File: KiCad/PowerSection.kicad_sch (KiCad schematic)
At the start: 28 parts, among them U2 MC34063AP, U3 LM7805_TO220, U4 LM337_TO220, U7 LM317_TO-220

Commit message: Changed footprints, arrangement of elements on pcb
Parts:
- removed R4, R46: 860, Resistor_SMD:R_0805_2012Metric_Pad1.20x1.40mm_HandSolder, symbol Device:R
- added R4, R46: 1k, Potentiometer_SMD:Potentiometer_Bourns_TC33X_Vertical, symbol Device:R_Variable
- C11, C12, C9: footprint Capacitor_SMD:CP_Elec_6.3x5.3 -> Capacitor_THT:CP_Radial_D5.0mm_P2.00mm
- C2, C4: footprint Capacitor_SMD:CP_Elec_6.3x7.7 -> Capacitor_THT:CP_Radial_D8.0mm_P3.50mm
- C6: footprint Capacitor_SMD:C_0805_2012Metric_Pad1.18x1.45mm_HandSolder -> Capacitor_THT:CP_Radial_D5.0mm_P2.00mm
- D2, D6, D7, D8: footprint Diode_SMD:D_SOD-123F -> Diode_THT:D_DO-41_SOD81_P10.16mm_Horizontal
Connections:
- net GND: now also R4.1, R46.2
- net at C6.1, D7.2 (A), R45.1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: now also R46.1
- net at C9.2, D8.1 (K), R5.2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: now also R4.2
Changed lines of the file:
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@@
 			)
 		)
-		(property "Footprint" "Capacitor_SMD:C_0805_2012Metric_Pad1.18x1.45mm_HandSolder"
+		(property "Footprint" "Capacitor_THT:CP_Radial_D5.0mm_P2.00mm"
 			(at 233.3752 91.44 0)
 			(effects
@@
 				(path "/e2db369b-fed9-4358-b449-15db5155edf2/27026b69-1c54-41be-a6f6-95a262163c29"
 					(reference "C10")
+					(unit 1)
+				)
+			)
+		)
+	)
+	(symbol
+		(lib_id "Device:R_Variable")
+		(at 209.55 119.38 0)
+		(unit 1)
+		(exclude_from_sim no)
+		(in_bom yes)
+		(on_board yes)
+		(dnp no)
+		(fields_autoplaced yes)
+		(property "Reference" "R4"
+			(at 213.36 118.1099 0)
+			(effects
+				(font
+					(size 1.27 1.27)
+				)
+				(justify left)
+			)
+		)
+		(property "Value" "1k"
+			(at 213.36 120.6499 0)
+			(effects
+				(font
+					(size 1.27 1.27)
+				)
+				(justify left)
+			)
+		)
+		(property "Footprint" "Potentiometer_SMD:Potentiometer_Bourns_TC33X_Vertical"
+			(at 207.772 119.38 90)
+			(effects
+				(font
+					(size 1.27 1.27)
+				)
+				(hide yes)
+			)
+		)
+		(property "Datasheet" "~"
+			(at 209.55 119.38 0)
+			(effects
+				(font
+					(size 1.27 1.27)
+				)
+				(hide yes)
+			)
+		)
+		(property "Description" "Variable resistor"
+			(at 209.55 119.38 0)
+			(effects
+				(font
+					(size 1.27 1.27)
+				)
+				(hide yes)
+			)
+		)
+		(pin "1"
+		)
+		(pin "2"
+		)
+		(instances
+			(project "SiganlGen"
+				(path "/e2db369b-fed9-4358-b449-15db5155edf2/27026b69-1c54-41be-a6f6-95a262163c29"
+					(reference "R4")
 					(unit 1)
 				)
@@
 	)
 	(symbol
-		(lib_id "Device:R")
-		(at 209.55 119.38 180)
-		(unit 1)
-		(exclude_from_sim no)
-		(in_bom yes)
-		(on_board yes)
-		(dnp no)
-		(fields_autoplaced yes)
-		(property "Reference" "R4"
-			(at 212.09 118.1099 0)
-			(effects
-				(font
-					(size 1.27 1.27)
-				)
-				(justify right)
-			)
-		)
-		(property "Value" "860"
-			(at 212.09 120.6499 0)
-			(effects
-				(font
-					(size 1.27 1.27)
-				)
-				(justify right)
-			)
-		)
-		(property "Footprint" "Resistor_SMD:R_0805_2012Metric_Pad1.20x1.40mm_HandSolder"
-			(at 211.328 119.38 90)
-			(effects
-				(font
-					(size 1.27 1.27)
-				)
-				(hide yes)
-			)
-		)
-		(property "Datasheet" "~"
-			(at 209.55 119.38 0)
-			(effects
-				(font
-					(size 1.27 1.27)
-				)
-				(hide yes)
-			)
-		)
-		(property "Description" "Resistor"
-			(at 209.55 119.38 0)
-			(effects
-				(font
-					(size 1.27 1.27)
-				)
-				(hide yes)
-			)
-		)
-		(pin "1"
-		)
-		(pin "2"
-		)
-		(instances
-			(project "SiganlGen"
-				(path "/e2db369b-fed9-4358-b449-15db5155edf2/27026b69-1c54-41be-a6f6-95a262163c29"
-					(reference "R4")
-					(unit 1)
-				)
-			)
-		)
-	)
-	(symbol
 		(lib_id "Device:C")
 		(at 104.14 111.76 0)
@@
 			)
 		)
-		(property "Footprint" "Capacitor_SMD:CP_Elec_6.3x5.3"
+		(property "Footprint" "Capacitor_THT:CP_Radial_D5.0mm_P2.00mm"
 			(at 246.0752 86.36 0)
 			(effects
@@
 			)
 		)
-		(property "Footprint" "Diode_SMD:D_SOD-123F"
+		(property "Footprint" "Diode_THT:D_DO-41_SOD81_P10.16mm_Horizontal"
 			(at 209.55 64.135 0)
 			(effects
@@
 			)
 		)
-		(property "Footprint" "Capacitor_SMD:CP_Elec_6.3x7.7"
+		(property "Footprint" "Capacitor_THT:CP_Radial_D8.0mm_P3.50mm"
 			(at 89.8652 102.87 0)
 			(effects
@@
 	)
 	(symbol
-		(lib_id "Device:R")
-		(at 209.55 88.9 180)
+		(lib_id "Device:R_Variable")
+		(at 209.55 88.9 0)
 		(unit 1)
 		(exclude_from_sim no)
@@
 		(fields_autoplaced yes)
 		(property "Reference" "R46"
-			(at 212.09 87.6299 0)
-			(effects
-				(font
-					(size 1.27 1.27)
-				)
-				(justify right)
-			)
-		)
-		(property "Value" "860"
-			(at 212.09 90.1699 0)
-			(effects
-				(font
-					(size 1.27 1.27)
-				)
-				(justify right)
-			)
-		)
-		(property "Footprint" "Resistor_SMD:R_0805_2012Metric_Pad1.20x1.40mm_HandSolder"
-			(at 211.328 88.9 90)
+			(at 213.36 87.6299 0)
+			(effects
+				(font
+					(size 1.27 1.27)
+				)
+				(justify left)
+			)
+		)
+		(property "Value" "1k"
+			(at 213.36 90.1699 0)
+			(effects
+				(font
+					(size 1.27 1.27)
+				)
+				(justify left)
+			)
+		)
+		(property "Footprint" "Potentiometer_SMD:Potentiometer_Bourns_TC33X_Vertical"
+			(at 207.772 88.9 90)
 			(effects
 				(font
@@
 			)
 		)
-		(property "Description" "Resistor"
+		(property "Description" "Variable resistor"
 			(at 209.55 88.9 0)
 			(effects
@@
 			)
 		)
-		(property "Footprint" "Diode_SMD:D_SOD-123F"
+		(property "Footprint" "Diode_THT:D_DO-41_SOD81_P10.16mm_Horizontal"
 			(at 227.965 77.47 0)
 			(effects
@@
 			)
 		)
-		(property "Footprint" "Diode_SMD:D_SOD-123F"
+		(property "Footprint" "Diode_THT:D_DO-41_SOD81_P10.16mm_Horizontal"
 			(at 227.965 130.81 0)
 			(effects
@@
 			)
 		)
-		(property "Footprint" "Diode_SMD:D_SOD-123F"
+		(property "Footprint" "Diode_THT:D_DO-41_SOD81_P10.16mm_Horizontal"
 			(at 207.01 142.875 0)
 			(effects
@@
 			)
 		)
-		(property "Footprint" "Capacitor_SMD:CP_Elec_6.3x7.7"
+		(property "Footprint" "Capacitor_THT:CP_Radial_D8.0mm_P3.50mm"
 			(at 149.5552 123.19 0)
 			(effects
@@
 			)
 		)
-		(property "Footprint" "Capacitor_SMD:CP_Elec_6.3x5.3"
+		(property "Footprint" "Capacitor_THT:CP_Radial_D5.0mm_P2.00mm"
 			(at 246.0752 130.81 0)
 			(effects
@@
 			)
 		)
-		(property "Footprint" "Capacitor_SMD:CP_Elec_6.3x5.3"
+		(property "Footprint" "Capacitor_THT:CP_Radial_D5.0mm_P2.00mm"
 			(at 233.3752 123.19 0)
 			(effects

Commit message: Tidied up schematic, changed footprints
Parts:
- D2, D6, D7, D8: footprint Diode_THT:D_DO-41_SOD81_P10.16mm_Horizontal -> Diode_SMD:D_SOD-123F
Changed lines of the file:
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@@
 			)
 		)
-		(property "Footprint" "Diode_THT:D_DO-41_SOD81_P10.16mm_Horizontal"
+		(property "Footprint" "Diode_SMD:D_SOD-123F"
 			(at 209.55 64.135 0)
 			(effects
@@
 			)
 		)
-		(property "Footprint" "Diode_THT:D_DO-41_SOD81_P10.16mm_Horizontal"
+		(property "Footprint" "Diode_SMD:D_SOD-123F"
 			(at 227.965 77.47 0)
 			(effects
@@
 			)
 		)
-		(property "Footprint" "Diode_THT:D_DO-41_SOD81_P10.16mm_Horizontal"
+		(property "Footprint" "Diode_SMD:D_SOD-123F"
 			(at 227.965 130.81 0)
 			(effects
@@
 			)
 		)
-		(property "Footprint" "Diode_THT:D_DO-41_SOD81_P10.16mm_Horizontal"
+		(property "Footprint" "Diode_SMD:D_SOD-123F"
 			(at 207.01 142.875 0)
 			(effects

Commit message: Alfa version of PCB design
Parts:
- removed C11, C12: 22u, Capacitor_THT:CP_Radial_D5.0mm_P2.00mm, symbol Device:C
- removed C2, C4: 220u, Capacitor_THT:CP_Radial_D8.0mm_P3.50mm, symbol Device:C
- added C11, C12, C13, C17: 100u, Capacitor_THT:CP_Radial_D5.0mm_P2.50mm, symbol Device:C_Polarized
- C6, C9: value 22u -> 10u; footprint Capacitor_THT:CP_Radial_D5.0mm_P2.00mm -> Capacitor_SMD:C_0805_2012Metric_Pad1.18x1.45mm_HandSolder
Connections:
- net +10V: now also C11.1
- net +12V: now also C17.1
- net -10V: now also C13.2
- net -12V: now also C12.2
- net GND: now also C11.2, C12.1, C13.1, C17.2

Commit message: PCB design
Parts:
- renumbered C9 to C10, C13 to C12, C5 to C2, C8 to C3, C17 to C4, C3 to C5, C12 to C6, C10 to C7, C7 to C8, C6 to C9, D1 to D2, D2 to D3, D6 to D4, D7 to D5, D8 to D6, R46 to R4, R4 to R5, R45 to R6, R5 to R7, U3 to U2, U2 to U3, U7 to U4, U4 to U5
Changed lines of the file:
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@@
 		(dnp no)
 		(fields_autoplaced yes)
-		(property "Reference" "U7"
+		(property "Reference" "U4"
 			(at 209.55 63.5 0)
 			(effects
@@
 			(project "SiganlGen"
 				(path "/e2db369b-fed9-4358-b449-15db5155edf2/27026b69-1c54-41be-a6f6-95a262163c29"
-					(reference "U7")
+					(reference "U4")
 					(unit 1)
 				)
@@
 		(dnp no)
 		(fields_autoplaced yes)
-		(property "Reference" "C6"
+		(property "Reference" "C9"
 			(at 236.22 86.3599 0)
 			(effects
@@
 			(project "SiganlGen"
 				(path "/e2db369b-fed9-4358-b449-15db5155edf2/27026b69-1c54-41be-a6f6-95a262163c29"
-					(reference "C6")
+					(reference "C9")
 					(unit 1)
 				)
@@
 		(on_board yes)
 		(dnp no)
-		(property "Reference" "C10"
+		(property "Reference" "C7"
 			(at 191.008 81.28 0)
 			(effects
@@
 			(project "SiganlGen"
 				(path "/e2db369b-fed9-4358-b449-15db5155edf2/27026b69-1c54-41be-a6f6-95a262163c29"
-					(reference "C10")
+					(reference "C7")
 					(unit 1)
 				)
@@
 		(dnp no)
 		(fields_autoplaced yes)
-		(property "Reference" "R4"
+		(property "Reference" "R5"
 			(at 213.36 118.1099 0)
 			(effects
@@
 			(project "SiganlGen"
 				(path "/e2db369b-fed9-4358-b449-15db5155edf2/27026b69-1c54-41be-a6f6-95a262163c29"
-					(reference "R4")
+					(reference "R5")
 					(unit 1)
 				)
@@
 		(on_board yes)
 		(dnp no)
-		(property "Reference" "U4"
+		(property "Reference" "U5"
 			(at 209.55 140.97 0)
 			(effects
@@
 			(project "SiganlGen"
 				(path "/e2db369b-fed9-4358-b449-15db5155edf2/27026b69-1c54-41be-a6f6-95a262163c29"
-					(reference "U4")
+					(reference "U5")
 					(unit 1)
 				)
@@
 		(on_board yes)
 		(dnp no)
-		(property "Reference" "C7"
+		(property "Reference" "C8"
 			(at 191.008 125.73 0)
 			(effects
@@
 			(project "SiganlGen"
 				(path "/e2db369b-fed9-4358-b449-15db5155edf2/27026b69-1c54-41be-a6f6-95a262163c29"
-					(reference "C7")
+					(reference "C8")
 					(unit 1)
 				)
@@
 		(dnp no)
 		(fields_autoplaced yes)
-		(property "Reference" "R5"
+		(property "Reference" "R7"
 			(at 223.52 129.5399 0)
 			(effects
@@
 			(project "SiganlGen"
 				(path "/e2db369b-fed9-4358-b449-15db5155edf2/27026b69-1c54-41be-a6f6-95a262163c29"
-					(reference "R5")
+					(reference "R7")
 					(unit 1)
 				)
@@
 		(dnp no)
 		(fields_autoplaced yes)
-		(property "Reference" "C3"
+		(property "Reference" "C5"
 			(at 107.95 110.4899 0)
 			(effects
@@
 			(project "SiganlGen"
 				(path "/e2db369b-fed9-4358-b449-15db5155edf2/27026b69-1c54-41be-a6f6-95a262163c29"
-					(reference "C3")
+					(reference "C5")
 					(unit 1)
 				)
@@
 		(dnp no)
 		(fields_autoplaced yes)
-		(property "Reference" "U2"
+		(property "Reference" "U3"
 			(at 118.11 83.82 0)
 			(effects
@@
 			(project "SiganlGen"
 				(path "/e2db369b-fed9-4358-b449-15db5155edf2/27026b69-1c54-41be-a6f6-95a262163c29"
-					(reference "U2")
+					(reference "U3")
 					(unit 1)
 				)
@@
 		(dnp no)
 		(fields_autoplaced yes)
-		(property "Reference" "C13"
+		(property "Reference" "C12"
 			(at 248.92 124.8409 0)
 			(effects
@@
 			(project "SiganlGen"
 				(path "/e2db369b-fed9-4358-b449-15db5155edf2/27026b69-1c54-41be-a6f6-95a262163c29"
-					(reference "C13")
+					(reference "C12")
 					(unit 1)
 				)
@@
 		(dnp no)
 		(fields_autoplaced yes)
-		(property "Reference" "C8"
+		(property "Reference" "C3"
 			(at 69.85 104.1399 0)
 			(effects
@@
 			(project "SiganlGen"
 				(path "/e2db369b-fed9-4358-b449-15db5155edf2/27026b69-1c54-41be-a6f6-95a262163c29"
-					(reference "C8")
+					(reference "C3")
 					(unit 1)
 				)
@@
 		(dnp no)
 		(fields_autoplaced yes)
-		(property "Reference" "U3"
+		(property "Reference" "U2"
 			(at 53.34 92.71 0)
 			(effects
@@
 			(project "SiganlGen"
 				(path "/e2db369b-fed9-4358-b449-15db5155edf2/27026b69-1c54-41be-a6f6-95a262163c29"
-					(reference "U3")
+					(reference "U2")
 					(unit 1)
 				)
@@
 		(dnp no)
 		(fields_autoplaced yes)
-		(property "Reference" "D6"
+		(property "Reference" "D4"
 			(at 209.55 53.34 0)
 			(effects
@@
 			(project "SiganlGen"
 				(path "/e2db369b-fed9-4358-b449-15db5155edf2/27026b69-1c54-41be-a6f6-95a262163c29"
-					(reference "D6")
+					(reference "D4")
 					(unit 1)
 				)
@@
 		(dnp no)
 		(fields_autoplaced yes)
-		(property "Reference" "R46"
+		(property "Reference" "R4"
 			(at 213.36 87.6299 0)
 			(effects
@@
 			(project "SiganlGen"
 				(path "/e2db369b-fed9-4358-b449-15db5155edf2/27026b69-1c54-41be-a6f6-95a262163c29"
-					(reference "R46")
+					(reference "R4")
 					(unit 1)
 				)
@@
 		(on_board yes)
 		(dnp no)
-		(property "Reference" "C12"
+		(property "Reference" "C6"
 			(at 143.51 122.936 0)
 			(effects
@@
 			(project "SiganlGen"
 				(path "/e2db369b-fed9-4358-b449-15db5155edf2/27026b69-1c54-41be-a6f6-95a262163c29"
-					(reference "C12")
+					(reference "C6")
 					(unit 1)
 				)
@@
 		(dnp no)
 		(fields_autoplaced yes)
-		(property "Reference" "D7"
+		(property "Reference" "D5"
 			(at 234.95 76.1999 90)
 			(effects
@@
 			(project "SiganlGen"
 				(path "/e2db369b-fed9-4358-b449-15db5155edf2/27026b69-1c54-41be-a6f6-95a262163c29"
-					(reference "D7")
+					(reference "D5")
 					(unit 1)
 				)
@@
 		(dnp no)
 		(fields_autoplaced yes)
-		(property "Reference" "D8"
+		(property "Reference" "D6"
 			(at 234.95 129.5399 90)
 			(effects
@@
 			(project "SiganlGen"
 				(path "/e2db369b-fed9-4358-b449-15db5155edf2/27026b69-1c54-41be-a6f6-95a262163c29"
-					(reference "D8")
+					(reference "D6")
 					(unit 1)
 				)
@@
 		(on_board yes)
 		(dnp no)
-		(property "Reference" "C5"
+		(property "Reference" "C2"
 			(at 42.672 103.886 0)
 			(effects
@@
 			(project "SiganlGen"
 				(path "/e2db369b-fed9-4358-b449-15db5155edf2/27026b69-1c54-41be-a6f6-95a262163c29"
-					(reference "C5")
+					(reference "C2")
 					(unit 1)
 				)
@@
 		(on_board yes)
 		(dnp no)
-		(property "Reference" "D2"
+		(property "Reference" "D3"
 			(at 210.82 148.59 0)
 			(effects
@@
 			(project "SiganlGen"
 				(path "/e2db369b-fed9-4358-b449-15db5155edf2/27026b69-1c54-41be-a6f6-95a262163c29"
-					(reference "D2")
+					(reference "D3")
 					(unit 1)
 				)
@@
 		(dnp no)
 		(fields_autoplaced yes)
-		(property "Reference" "D1"
+		(property "Reference" "D2"
 			(at 147.0025 95.25 0)
 			(effects
@@
 			(project "SiganlGen"
 				(path "/e2db369b-fed9-4358-b449-15db5155edf2/27026b69-1c54-41be-a6f6-95a262163c29"
-					(reference "D1")
+					(reference "D2")
 					(unit 1)
 				)
@@
 		(dnp no)
 		(fields_autoplaced yes)
-		(property "Reference" "R45"
+		(property "Reference" "R6"
 			(at 223.52 74.9299 0)
 			(effects
@@
 			(project "SiganlGen"
 				(path "/e2db369b-fed9-4358-b449-15db5155edf2/27026b69-1c54-41be-a6f6-95a262163c29"
-					(reference "R45")
+					(reference "R6")
 					(unit 1)
 				)
@@
 		(on_board yes)
 		(dnp no)
-		(property "Reference" "C9"
+		(property "Reference" "C10"
 			(at 235.458 118.364 0)
 			(effects
@@
 			(project "SiganlGen"
 				(path "/e2db369b-fed9-4358-b449-15db5155edf2/27026b69-1c54-41be-a6f6-95a262163c29"
-					(reference "C9")
+					(reference "C10")
 					(unit 1)
 				)
@@
 		(dnp no)
 		(fields_autoplaced yes)
-		(property "Reference" "C17"
+		(property "Reference" "C4"
 			(at 92.71 96.9009 0)
 			(effects
@@
 			(project "SiganlGen"
 				(path "/e2db369b-fed9-4358-b449-15db5155edf2/27026b69-1c54-41be-a6f6-95a262163c29"
-					(reference "C17")
-					(unit 1)
-				)
+					(reference "C4")
+					(unit 1)
+				)

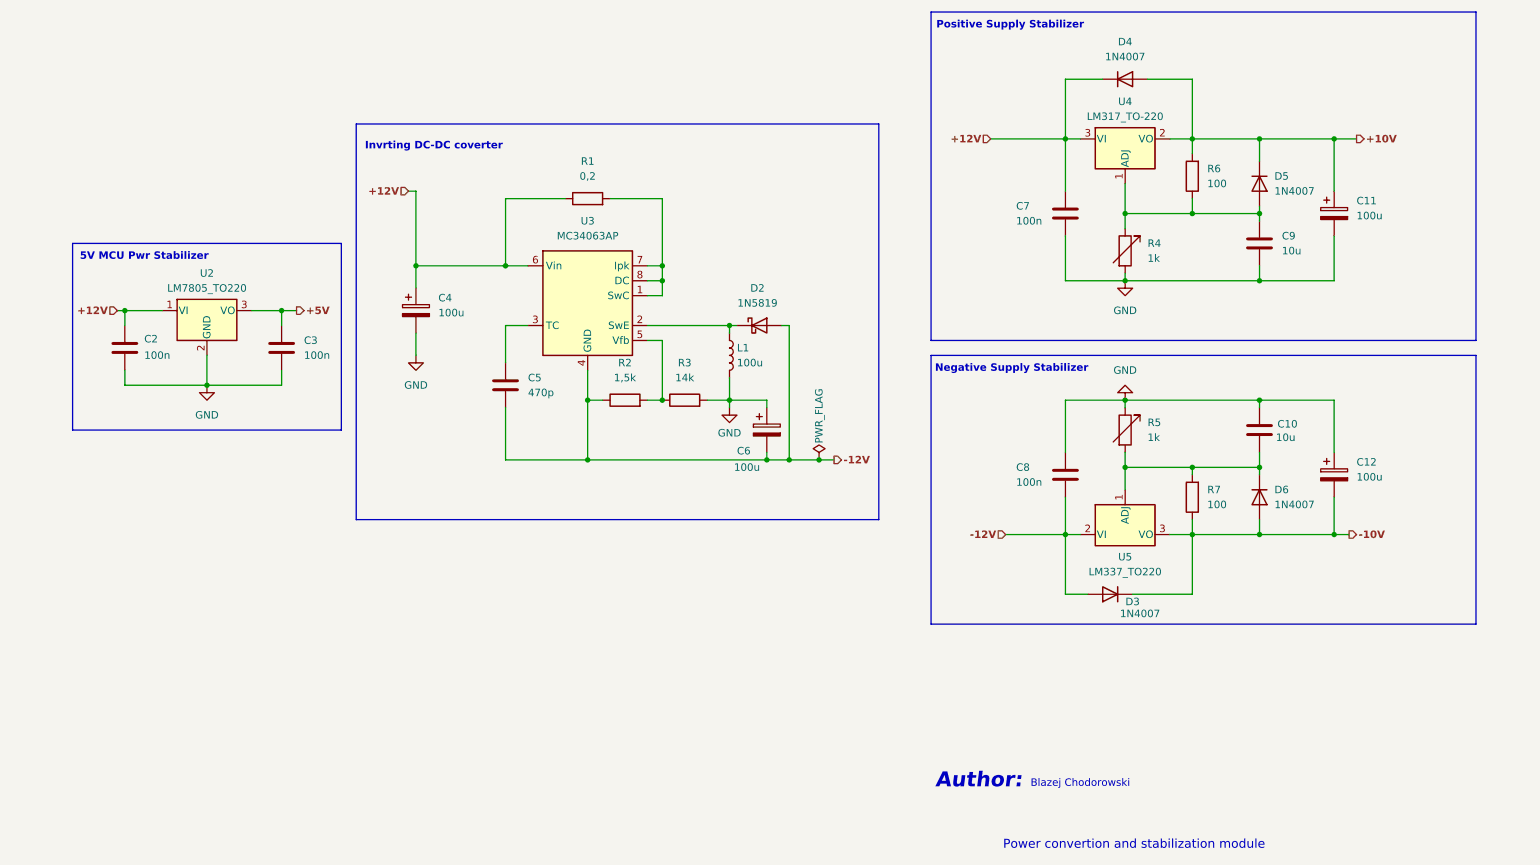
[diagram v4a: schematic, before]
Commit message: output sim, filter sim, filter sch, output change
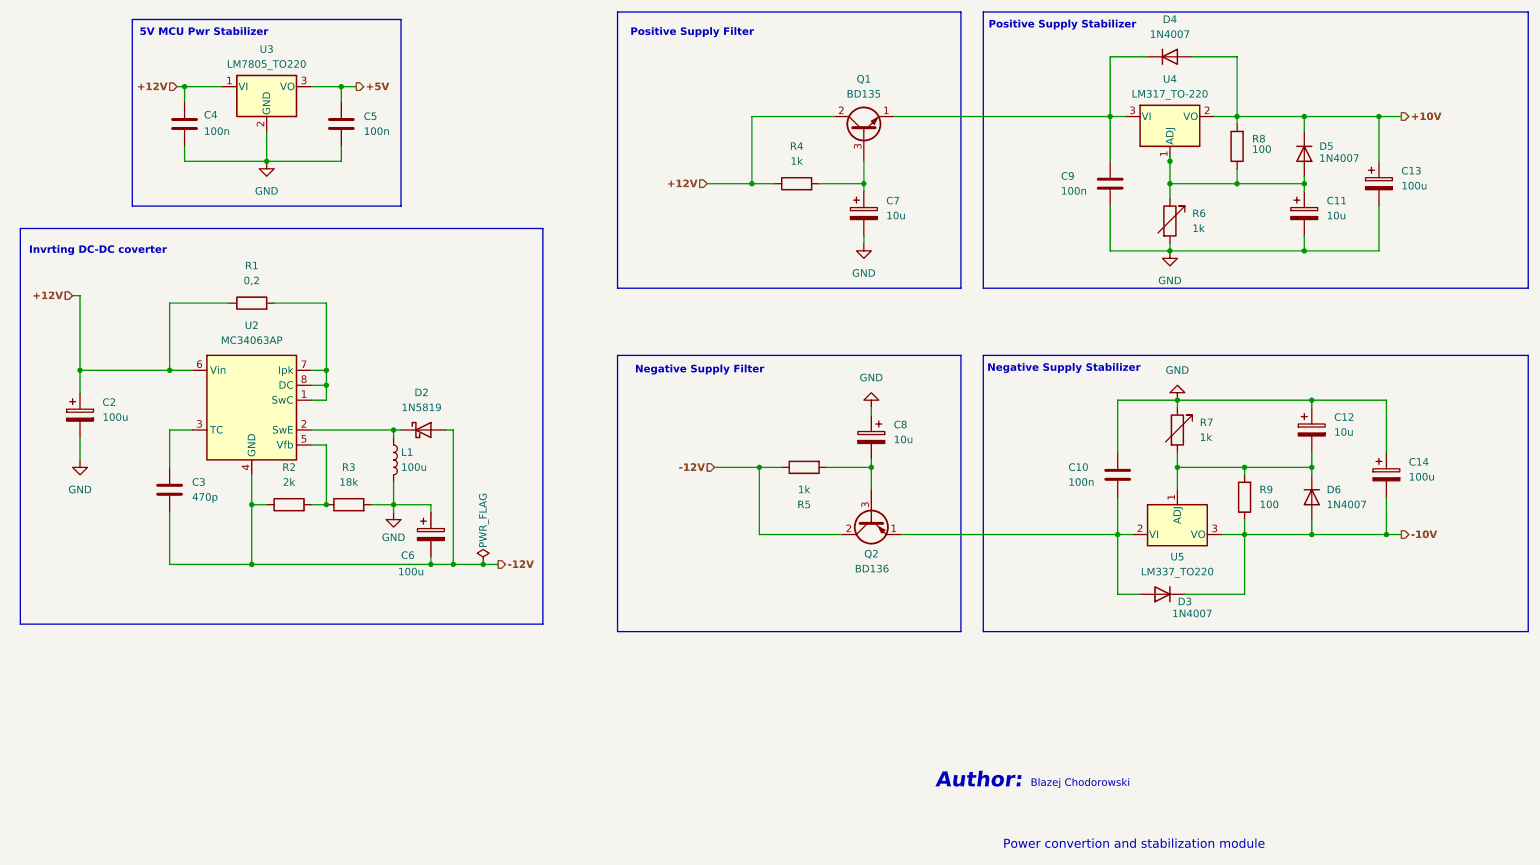
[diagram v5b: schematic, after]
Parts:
- removed C10, C9: 10u, Capacitor_SMD:C_0805_2012Metric_Pad1.18x1.45mm_HandSolder, symbol Device:C
- added C11, C12, C7, C8: 10u, symbol Device:C_Polarized
- added Q1: BD135, Package_TO_SOT_THT:TO-126-3_Vertical, symbol Transistor_BJT:BD135
- added Q2: BD136, Package_TO_SOT_THT:TO-126-3_Vertical, symbol Transistor_BJT:BD136
- added R4, R5: 1k, symbol Device:R
- R2: value 1,5k -> 2k
- R3: value 14k -> 18k
- renumbered C8 to C10, C11 to C13, C12 to C14, C4 to C2, C5 to C3, C2 to C4, C3 to C5, C7 to C9, R4 to R6, R5 to R7, R6 to R8, R7 to R9, U3 to U2, U2 to U3
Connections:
- net +12V: now also Q1.2 (C), R4.1; no longer C9.1, D4.1 (K), U4.3 (VI)
- net -12V: now also Q2.2 (C), R5.1; no longer C10.2, D3.2 (A), U5.2 (VI)
- net GND: now also C11.2, C12.1, C7.2, C8.1
- net at D5.2 (A), R6.1, R8.1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: now also C11.1
- net at D6.1 (K), R7.2, R9.2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: now also C12.2
- new net: C9.1, D4.1 (K), Q1.1 (E), U4.3 (VI)
- new net: C7.1, Q1.3 (B), R4.2
- new net: C10.2, D3.2 (A), Q2.1 (E), U5.2 (VI)
- new net: C8.2, Q2.3 (B), R5.2
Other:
- note added: "Negative Supply Filter"
- note added: "Positive Supply Filter"
- moved on the sheet: C10, C13, C14, C2, C3, C4, C5, C6, C9, D2, D3, D4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

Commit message: Updated footprints
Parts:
- C11, C12, C7, C8: footprint (none) -> Capacitor_THT:CP_Radial_D5.0mm_P2.00mm
- R4, R5: footprint (none) -> Resistor_SMD:R_0805_2012Metric_Pad1.20x1.40mm_HandSolder
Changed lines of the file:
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@@
 			)
 		)
-		(property "Footprint" ""
+		(property "Footprint" "Capacitor_THT:CP_Radial_D5.0mm_P2.00mm"
 			(at 242.2652 123.19 0)
 			(effects
@@
 			)
 		)
-		(property "Footprint" ""
+		(property "Footprint" "Resistor_SMD:R_0805_2012Metric_Pad1.20x1.40mm_HandSolder"
 			(at 153.67 79.248 90)
 			(effects
@@
 			)
 		)
-		(property "Footprint" ""
+		(property "Footprint" "Capacitor_THT:CP_Radial_D5.0mm_P2.00mm"
 			(at 240.9952 86.36 0)
 			(effects
@@
 			)
 		)
-		(property "Footprint" ""
+		(property "Footprint" "Capacitor_THT:CP_Radial_D5.0mm_P2.00mm"
 			(at 166.0652 86.36 0)
 			(effects
@@
 			)
 		)
-		(property "Footprint" ""
+		(property "Footprint" "Resistor_SMD:R_0805_2012Metric_Pad1.20x1.40mm_HandSolder"
 			(at 154.94 123.952 90)
 			(effects
@@
 			)
 		)
-		(property "Footprint" ""
+		(property "Footprint" "Capacitor_THT:CP_Radial_D5.0mm_P2.00mm"
 			(at 165.4048 124.46 0)
 			(effects
